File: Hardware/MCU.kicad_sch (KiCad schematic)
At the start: 0 parts

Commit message: Added cheapest STM32L0 from mouser and mapped USART UART SPI and I2C to headers
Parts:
- added C18: 10uF, symbol Device:C
- added C20: 100nF, symbol Device:C
- added J1: Serial Wire Debug(SWD), symbol Connector_Generic:Conn_01x06
- added J2: Conn_01x07 USART2, symbol Connector_Generic:Conn_01x07
- added J3: Conn_01x07 LPUART1, symbol Connector_Generic:Conn_01x07
- added J4: Conn_01x08 SPI1, symbol Connector_Generic:Conn_01x08
- added J5: Conn_01x05 I2C, symbol Connector_Generic:Conn_01x05
- added JP10, JP2, JP3, JP4, JP5, JP6, JP7, JP8, JP9: SolderJumper_3_Open, symbol Jumper:SolderJumper_3_Open
- added JP11, JP17: SPI1_MISO AF0, symbol Jumper:SolderJumper_2_Open
- added JP12: SPI1_MOSI AF0, symbol Jumper:SolderJumper_2_Open
- added JP13: SPI1_NSS AF0, symbol Jumper:SolderJumper_2_Open
- added JP14: SPI1_SCK AF0, symbol Jumper:SolderJumper_2_Open
- added JP15: SPI1_MOSI AF1, symbol Jumper:SolderJumper_2_Open
- added JP16: SPI1_SCK AF5, symbol Jumper:SolderJumper_2_Open
- added JP18: I2C_SCL AF1, symbol Jumper:SolderJumper_2_Open
- added JP19: I2C_SDA AF1, symbol Jumper:SolderJumper_2_Open
- added JP20: USART2_RX AF0, symbol Jumper:SolderJumper_2_Open
- added JP21, JP22: USART2_RX AF4, symbol Jumper:SolderJumper_2_Open
- added JP23: USART2_CK AF0, symbol Jumper:SolderJumper_2_Open
- added JP24: USART2_CK AF4, symbol Jumper:SolderJumper_2_Open
- added JP25, JP26, JP27: USART2_TX AF4, symbol Jumper:SolderJumper_2_Open
- added JP28, JP29: USART2_CTS AF4, symbol Jumper:SolderJumper_2_Open
- added JP30: USART2_RTS AF4, symbol Jumper:SolderJumper_2_Open
- added JP31: LPUART1_CTS AF4, symbol Jumper:SolderJumper_2_Open
- added JP32: LPUART1_RTS AF4, symbol Jumper:SolderJumper_2_Open
- added JP33, JP34, JP35: LPUART1_RX AF6, symbol Jumper:SolderJumper_2_Open
- added JP36, JP37, JP38, JP39: LPUART1_TX AF6, symbol Jumper:SolderJumper_2_Open
- added JP40, JP43: I2C_SMBA AF3, symbol Jumper:SolderJumper_2_Open
- added JP41: I2C_SCL AF3, symbol Jumper:SolderJumper_2_Open
- added JP42: I2C_SDA AF3, symbol Jumper:SolderJumper_2_Open
- added U6: STM32L010F4Px, Package_SO:TSSOP-20_4.4x6.5mm_P0.65mm, symbol MCU_ST_STM32L0:STM32L010F4Px
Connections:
- new net +3V3: C18.1, C20.1, J1.1 (Pin_1), J2.1 (Pin_1), J3.1 (Pin_1), J4.1 (Pin_1), J5.1 (Pin_1), U6.16 (VDD), U6.5 (VDDA)
- new net GND: C18.2, C20.2, J1.3 (Pin_3), J2.7 (Pin_7), J3.7 (Pin_7), J4.8 (Pin_8), J5.5 (Pin_5), U6.15 (VSS)
- new net I2C_SCL: J5.2 (Pin_2), JP18.1 (A), JP41.1 (A)
- new net I2C_SDA: J5.3 (Pin_3), JP19.1 (A), JP42.1 (A)
- new net I2C_SMBA: J5.4 (Pin_4), JP40.1 (A), JP43.1 (A)
- new net IN Ref: JP10.1 (A), JP2.1 (A), JP3.1 (A), JP4.1 (A), JP5.1 (A), JP6.1 (A), JP7.1 (A), JP8.1 (A), JP9.1 (A)
- new net IN Signal: JP10.3 (B), JP2.3 (B), JP3.3 (B), JP4.3 (B), JP5.3 (B), JP6.3 (B), JP7.3 (B), JP8.3 (B), JP9.3 (B)
- new net LPUART1_CTS: J3.5 (Pin_5), JP31.1 (A)
- new net LPUART1_RTS: J3.4 (Pin_4), JP32.1 (A)
- new net LPUART1_RX: J3.3 (Pin_3), JP33.1 (A), JP34.1 (A), JP35.1 (A)
- new net LPUART1_TX: J3.2 (Pin_2), JP36.1 (A), JP37.1 (A), JP38.1 (A), JP39.1 (A)
- new net NRST: J1.5 (Pin_5), U6.4 (NRST)
- new net PA0 A0: JP2.2 (C), JP20.2 (B), JP28.2 (B), JP33.2 (B), U6.6 (PA0)
- new net PA1 A1: JP3.2 (C), JP30.2 (B), JP36.2 (B), JP43.2 (B), U6.7 (PA1)
- new net PA10: JP19.2 (B), JP22.2 (B), U6.18 (PA10)
- new net PA13 SWDIO: J1.4 (Pin_4), JP16.2 (B), JP35.2 (B), JP42.2 (B), U6.19 (PA13)
- new net PA14 SWCLK: J1.2 (Pin_2), JP17.2 (B), JP27.2 (B), JP39.2 (B), JP40.2 (B), U6.20 (PA14)
- new net PA2 A2: JP25.2 (B), JP37.2 (B), JP4.2 (C), U6.8 (PA2)
- new net PA3 A3: JP21.2 (B), JP34.2 (B), JP5.2 (C), U6.9 (PA3)
- new net PA4 A4: JP13.2 (B), JP24.2 (B), JP38.2 (B), JP41.2 (B), JP6.2 (C), U6.10 (PA4)
- new net PA5 A5: JP14.2 (B), JP7.2 (C), U6.11 (PA5)
- new net PA6 A6: JP11.2 (B), JP31.2 (B), JP8.2 (C), U6.12 (PA6)
- new net PA7 A7: JP12.2 (B), JP29.2 (B), JP9.2 (C), U6.13 (PA7)
- new net PA9: JP18.2 (B), JP26.2 (B), U6.17 (PA9)
- new net PB1 A9 VREF_OUT: JP10.2 (C), JP15.2 (B), JP23.2 (B), JP32.2 (B), U6.14 (PB1)
- new net PB9 Boot0: J1.6 (Pin_6), U6.1 (PB9)
- new net PC14 OSC32_IN: U6.2 (PC14)
- new net PC15 OSC32_OUT: U6.3 (PC15)
- new net SPI1_MISO: J4.4 (Pin_4), JP11.1 (A), JP17.1 (A)
- new net SPI1_MOSI: J4.3 (Pin_3), JP12.1 (A), JP15.1 (A)
- new net SPI1_NSS: J4.5 (Pin_5), JP13.1 (A)
- new net SPI1_SCK: J4.2 (Pin_2), JP14.1 (A), JP16.1 (A)
- new net USART2_CK: J2.6 (Pin_6), JP23.1 (A), JP24.1 (A)
- new net USART2_CTS: J2.5 (Pin_5), JP28.1 (A), JP29.1 (A)
- new net USART2_RTS: J2.4 (Pin_4), JP30.1 (A)
- new net USART2_RX: J2.3 (Pin_3), JP20.1 (A), JP21.1 (A), JP22.1 (A)
- new net USART2_TX: J2.2 (Pin_2), JP25.1 (A), JP26.1 (A), JP27.1 (A)
- no-connect marks 0 -> 1
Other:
- note added: "I2C1"
- note added: "LPUART1"
- note added: "MCU"
- note added: "SPI1"
- note added: "USART2"

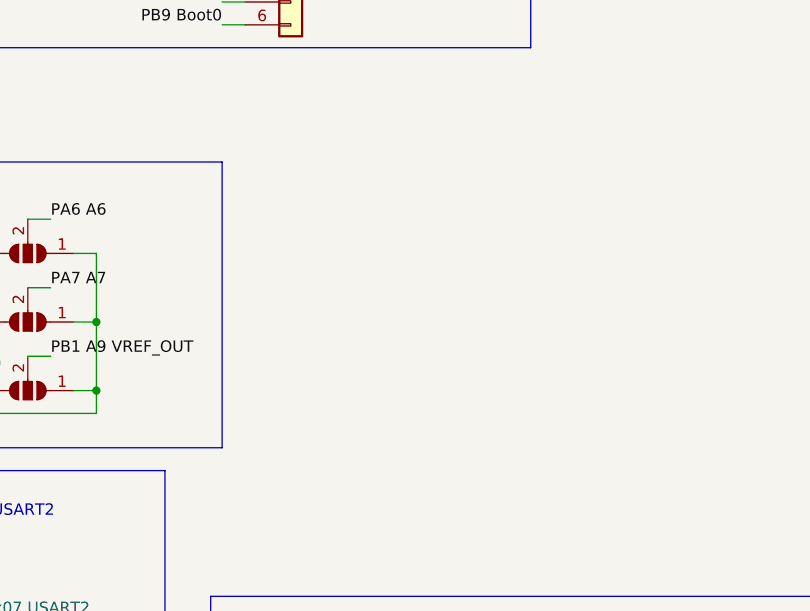
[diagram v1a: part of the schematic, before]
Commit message: Added reset button to mcu sheet
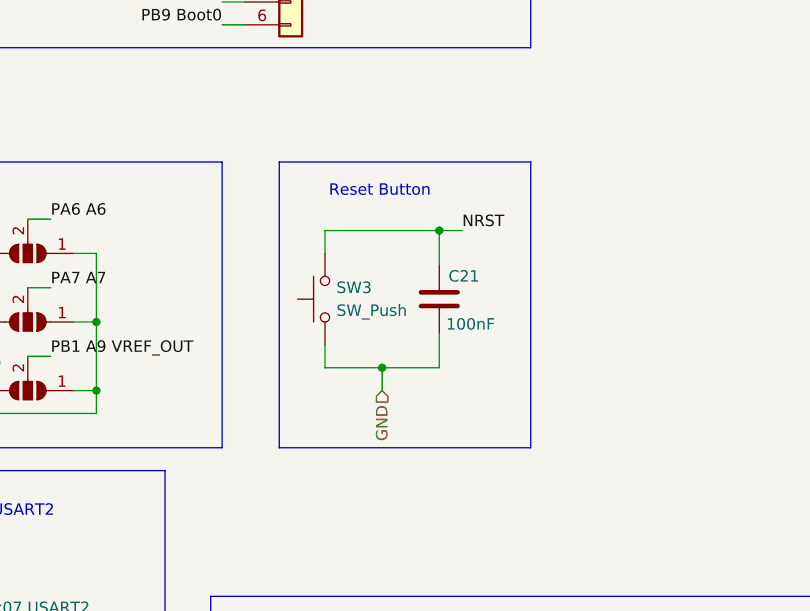
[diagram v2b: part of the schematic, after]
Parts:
- added C21: 100nF, symbol Device:C
- added SW3: SW_Push, symbol Switch:SW_Push
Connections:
- net GND: now also C21.2, SW3.1
- net NRST: now also C21.1, SW3.2
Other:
- note added: "Reset Button"

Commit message: Started linking footprints and work on the pcb layout
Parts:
- C18: footprint (none) -> Capacitor_SMD:C_0805_2012Metric_Pad1.18x1.45mm_HandSolder
- C20, C21: footprint (none) -> Capacitor_SMD:C_0402_1005Metric_Pad0.74x0.62mm_HandSolder
- J1: footprint (none) -> Connector_PinHeader_2.54mm:PinHeader_1x06_P2.54mm_Vertical
- J2, J3: footprint (none) -> Connector_PinHeader_2.54mm:PinHeader_1x07_P2.54mm_Vertical
- J4: footprint (none) -> Connector_PinHeader_2.54mm:PinHeader_1x08_P2.54mm_Vertical
- J5: footprint (none) -> Connector_PinHeader_2.54mm:PinHeader_1x05_P2.54mm_Vertical
- JP10, JP2, JP3, JP4, JP5, JP6, JP7, JP8, JP9: footprint (none) -> Jumper:SolderJumper-3_P1.3mm_Open_Pad1.0x1.5mm
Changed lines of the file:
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@@
 			)
 		)
-		(property "Footprint" ""
+		(property "Footprint" "Jumper:SolderJumper-3_P1.3mm_Open_Pad1.0x1.5mm"
 			(at 52.07 118.11 0)
 			(effects
@@
 			)
 		)
-		(property "Footprint" ""
+		(property "Footprint" "Jumper:SolderJumper-3_P1.3mm_Open_Pad1.0x1.5mm"
 			(at 52.07 102.87 0)
 			(effects
@@
 			)
 		)
-		(property "Footprint" ""
+		(property "Footprint" "Capacitor_SMD:C_0402_1005Metric_Pad0.74x0.62mm_HandSolder"
 			(at 113.9952 111.76 0)
 			(effects
@@
 			)
 		)
-		(property "Footprint" ""
+		(property "Footprint" "Jumper:SolderJumper-3_P1.3mm_Open_Pad1.0x1.5mm"
 			(at 36.83 110.49 0)
 			(effects
@@
 			)
 		)
-		(property "Footprint" ""
+		(property "Footprint" "Jumper:SolderJumper-3_P1.3mm_Open_Pad1.0x1.5mm"
 			(at 67.31 110.49 0)
 			(effects
@@
 			)
 		)
-		(property "Footprint" ""
+		(property "Footprint" "Capacitor_SMD:C_0805_2012Metric_Pad1.18x1.45mm_HandSolder"
 			(at 77.1652 34.29 0)
 			(effects
@@
 			)
 		)
-		(property "Footprint" ""
+		(property "Footprint" "Connector_PinHeader_2.54mm:PinHeader_1x07_P2.54mm_Vertical"
 			(at 53.34 140.97 0)
 			(effects
@@
 			)
 		)
-		(property "Footprint" ""
+		(property "Footprint" "Connector_PinHeader_2.54mm:PinHeader_1x05_P2.54mm_Vertical"
 			(at 251.46 111.76 0)
 			(effects
@@
 			)
 		)
-		(property "Footprint" ""
+		(property "Footprint" "Jumper:SolderJumper-3_P1.3mm_Open_Pad1.0x1.5mm"
 			(at 67.31 102.87 0)
 			(effects
@@
 			)
 		)
-		(property "Footprint" ""
+		(property "Footprint" "Connector_PinHeader_2.54mm:PinHeader_1x06_P2.54mm_Vertical"
 			(at 96.52 69.85 0)
 			(effects
@@
 			)
 		)
-		(property "Footprint" ""
+		(property "Footprint" "Capacitor_SMD:C_0402_1005Metric_Pad0.74x0.62mm_HandSolder"
 			(at 86.0552 34.29 0)
 			(effects
@@
 			)
 		)
-		(property "Footprint" ""
+		(property "Footprint" "Connector_PinHeader_2.54mm:PinHeader_1x08_P2.54mm_Vertical"
 			(at 248.92 143.51 0)
 			(effects
@@
 			)
 		)
-		(property "Footprint" ""
+		(property "Footprint" "Jumper:SolderJumper-3_P1.3mm_Open_Pad1.0x1.5mm"
 			(at 52.07 110.49 0)
 			(effects
@@
 			)
 		)
-		(property "Footprint" ""
+		(property "Footprint" "Jumper:SolderJumper-3_P1.3mm_Open_Pad1.0x1.5mm"
 			(at 36.83 102.87 0)
 			(effects
@@
 			)
 		)
-		(property "Footprint" ""
+		(property "Footprint" "Jumper:SolderJumper-3_P1.3mm_Open_Pad1.0x1.5mm"
 			(at 36.83 118.11 0)
 			(effects
@@
 			)
 		)
-		(property "Footprint" ""
+		(property "Footprint" "Connector_PinHeader_2.54mm:PinHeader_1x07_P2.54mm_Vertical"
 			(at 125.73 152.4 0)
 			(effects
@@
 			)
 		)
-		(property "Footprint" ""
+		(property "Footprint" "Jumper:SolderJumper-3_P1.3mm_Open_Pad1.0x1.5mm"
 			(at 67.31 118.11 0)
 			(effects

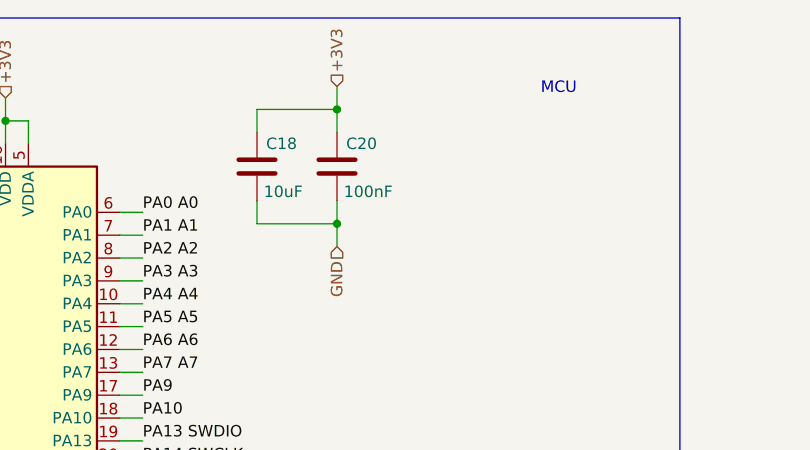
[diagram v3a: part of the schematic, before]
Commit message: added more footprints and continued on the circuit diagram
- [ ] add antenna connection
- [ ] find suitable 390Mohm resistor
- [ ] add switches, reset and power
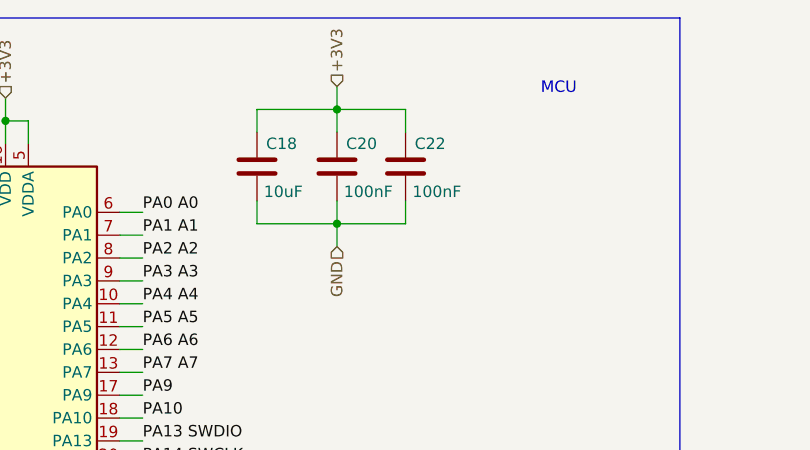
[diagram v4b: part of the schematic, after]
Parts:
- added C22: 100nF, Capacitor_SMD:C_0402_1005Metric_Pad0.74x0.62mm_HandSolder, symbol Device:C
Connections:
- net +3V3: now also C22.1
- net GND: now also C22.2
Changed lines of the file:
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@@
 	(wire
 		(pts
+			(xy 92.71 36.83) (xy 85.09 36.83)
+		)
+		(stroke
+			(width 0)
+			(type default)
+		)
+	)
+	(wire
+		(pts
 			(xy 59.69 110.49) (xy 59.69 118.11)
 		)
@@
 	(wire
 		(pts
+			(xy 92.71 24.13) (xy 85.09 24.13)
+		)
+		(stroke
+			(width 0)
+			(type default)
+		)
+	)
+	(wire
+		(pts
 			(xy 176.53 135.89) (xy 190.5 135.89)
 		)
@@
 	(wire
 		(pts
+			(xy 92.71 34.29) (xy 92.71 36.83)
+		)
+		(stroke
+			(width 0)
+			(type default)
+		)
+	)
+	(wire
+		(pts
 			(xy 41.91 118.11) (xy 44.45 118.11)
 		)
@@
 	(wire
 		(pts
+			(xy 92.71 26.67) (xy 92.71 24.13)
+		)
+		(stroke
+			(width 0)
+			(type default)
+		)
+	)
+	(wire
+		(pts
 			(xy 67.31 154.94) (xy 67.31 157.48)
 		)
@@
 		)
 	)
+	(symbol
+		(lib_id "Device:C")
+		(at 92.71 30.48 0)
+		(unit 1)
+		(exclude_from_sim no)
+		(in_bom yes)
+		(on_board yes)
+		(dnp no)
+		(property "Reference" "C22"
+			(at 93.726 27.94 0)
+			(effects
+				(font
+					(size 1.27 1.27)
+				)
+				(justify left)
+			)
+		)
+		(property "Value" "100nF"
+			(at 93.472 33.274 0)
+			(effects
+				(font
+					(size 1.27 1.27)
+				)
+				(justify left)
+			)
+		)
+		(property "Footprint" "Capacitor_SMD:C_0402_1005Metric_Pad0.74x0.62mm_HandSolder"
+			(at 93.6752 34.29 0)
+			(effects
+				(font
+					(size 1.27 1.27)
+				)
+				(hide yes)
+			)
+		)
+		(property "Datasheet" "~"
+			(at 92.71 30.48 0)
+			(effects
+				(font
+					(size 1.27 1.27)
+				)
+				(hide yes)
+			)
+		)
+		(property "Description" "Unpolarized capacitor"
+			(at 92.71 30.48 0)
+			(effects
+				(font
+					(size 1.27 1.27)
+				)
+				(hide yes)
+			)
+		)
+		(pin "2"
+		)
+		(pin "1"
+		)
+		(instances
+			(project "Hardware"
+				(path "/4e457c11-25d4-4677-9942-6ed7396aaf8a/9fe3c419-1bbf-4711-a173-31b4697dc050"
+					(reference "C22")
+					(unit 1)
+				)
+			)
+		)
+	)
